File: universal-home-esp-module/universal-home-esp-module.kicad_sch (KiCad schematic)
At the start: 1 part, among them U1 ESP32-C3_SUPERMINI_SMD

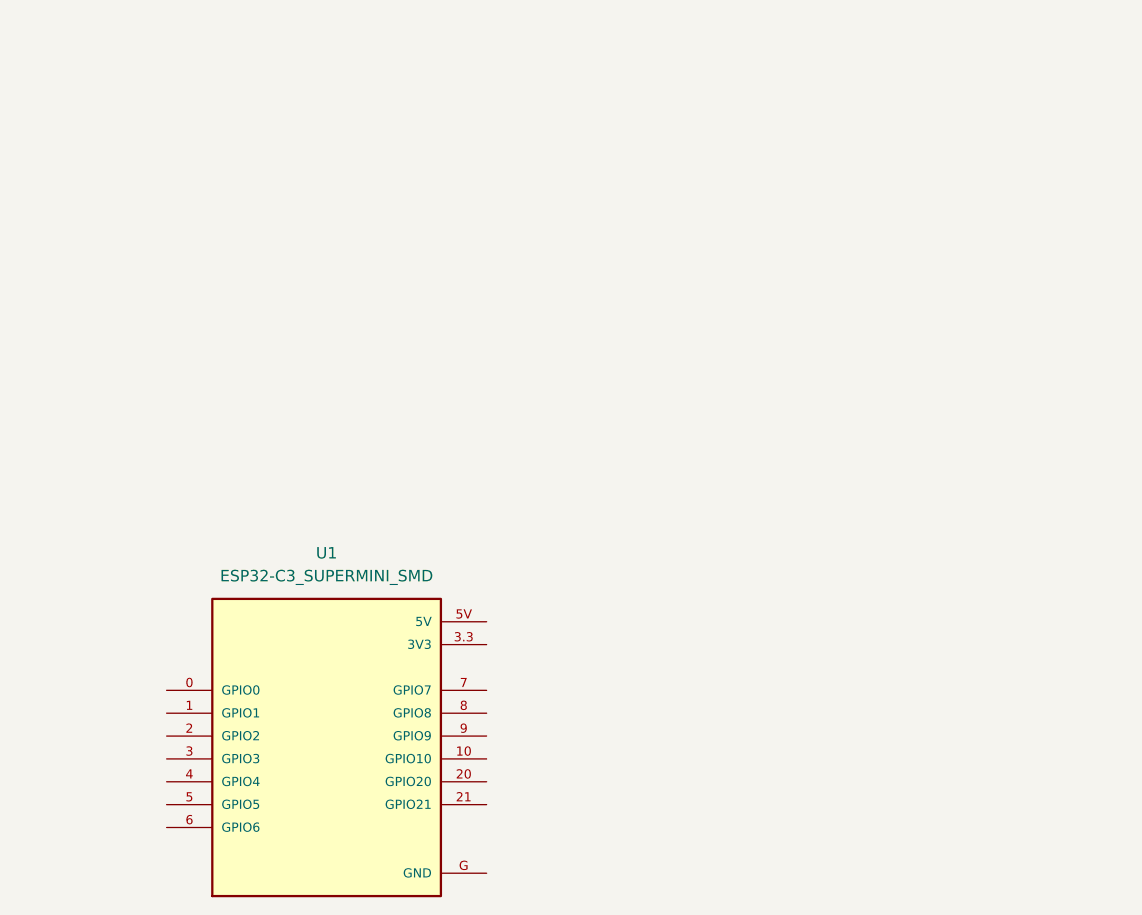
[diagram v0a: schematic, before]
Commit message: added required symbols in schematic, pending design
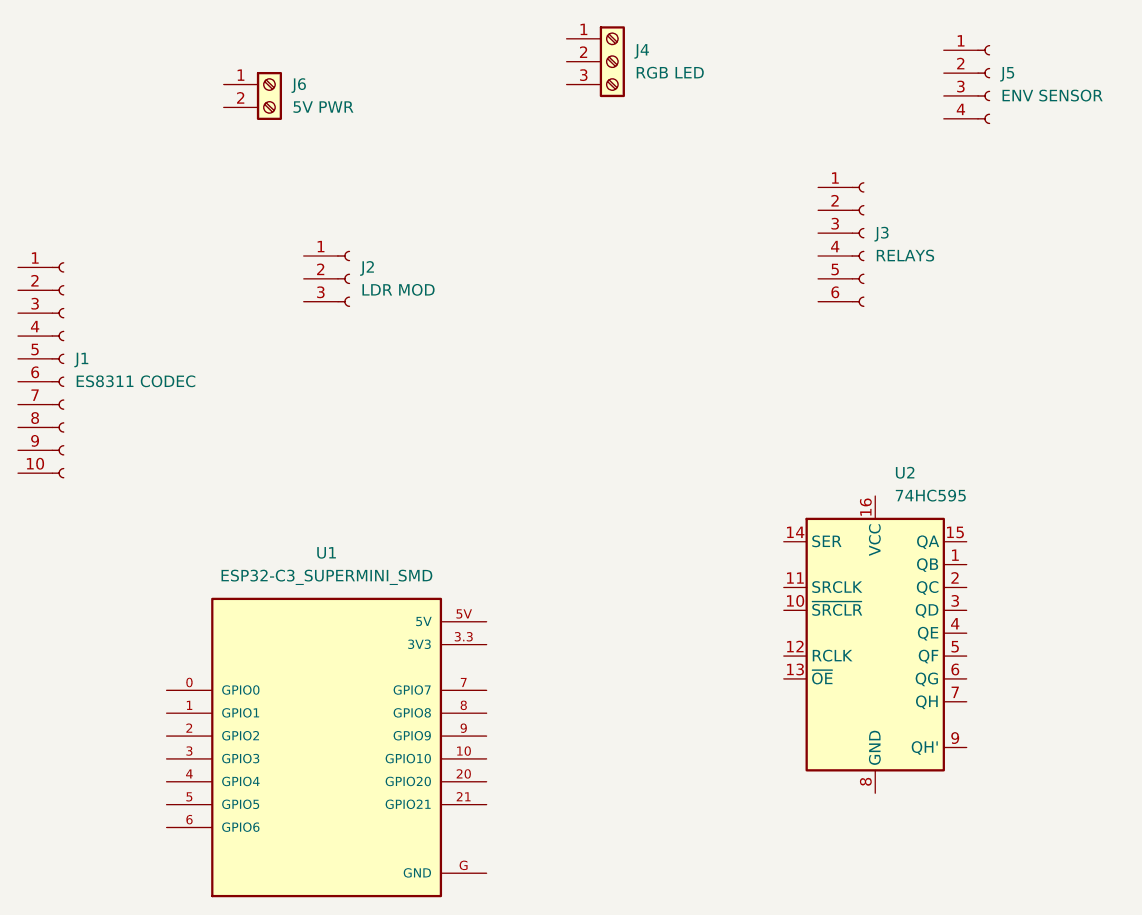
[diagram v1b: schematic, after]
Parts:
- added J1: ES8311 CODEC, Connector_PinHeader_2.54mm:PinHeader_1x10_P2.54mm_Vertical, symbol Connector:Conn_01x10_Socket
- added J2: LDR MOD, Connector_PinSocket_2.54mm:PinSocket_1x03_P2.54mm_Vertical, symbol Connector:Conn_01x03_Socket
- added J3: RELAYS, Connector_PinSocket_2.54mm:PinSocket_1x06_P2.54mm_Vertical, symbol Connector:Conn_01x06_Socket
- added J4: RGB LED, TerminalBlock_RND:TerminalBlock_RND_205-00233_1x03_P5.08mm_Horizontal, symbol Connector:Screw_Terminal_01x03
- added J5: ENV SENSOR, Connector_PinHeader_2.54mm:PinHeader_1x04_P2.54mm_Vertical, symbol Connector:Conn_01x04_Socket
- added J6: 5V PWR, TerminalBlock_RND:TerminalBlock_RND_205-00232_1x02_P5.08mm_Horizontal, symbol Connector:Screw_Terminal_01x02
- added U2: 74HC595, Package_DIP:DIP-16_W7.62mm_LongPads, symbol 74xx:74HC595

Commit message: updated schematic
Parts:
- added J7: EXT_GPIO, Connector_PinHeader_2.54mm:PinHeader_1x04_P2.54mm_Vertical, symbol Connector:Conn_01x04_Socket
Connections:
- net GND: now reaches J1.1 (Pin_1)
- net GND: now also J2.2 (Pin_2), J3.6 (Pin_6), J4.3 (Pin_3), J5.2 (Pin_2), J6.2 (Pin_2), U1.G (GND), U2.8 (GND)
- net 5V: now reaches J1.2 (Pin_2)
- net 5V: now also J6.1 (Pin_1), U1.5V
- net 3V3: now reaches J1.3 (Pin_3)
- net 3V3: now also J2.1 (Pin_1), J3.1 (Pin_1), J4.1 (Pin_1), J5.1 (Pin_1), U1.3.3 (3V3), U2.16 (VCC)
- net at U2.1 (QB): now also J3.3 (Pin_3)
- net at U2.15 (QA): now also J3.2 (Pin_2)
- net at U2.2 (QC): now also J3.4 (Pin_4)
- net at U2.3 (QD): now also J3.5 (Pin_5)
- net at U2.4 (QE): now also J7.1 (Pin_1)
- net at U2.5 (QF): now also J7.2 (Pin_2)
- net at U2.6 (QG): now also J7.3 (Pin_3)
- net at U2.7 (QH): now also J7.4 (Pin_4)
- no-connect marks 0 -> 1
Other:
- moved on the sheet: J1, J2, J3, J4, J5, J6, U2

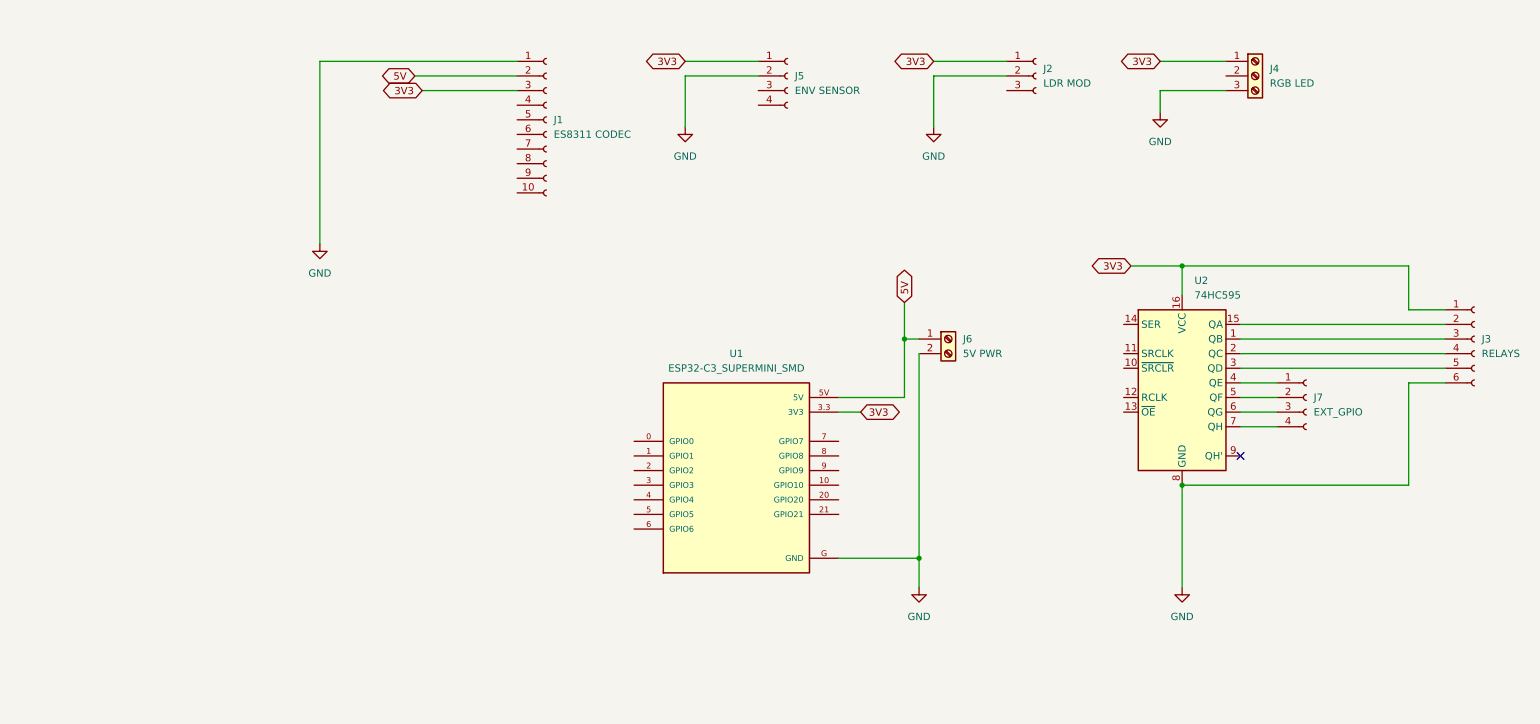
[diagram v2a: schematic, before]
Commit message: finalized schematic
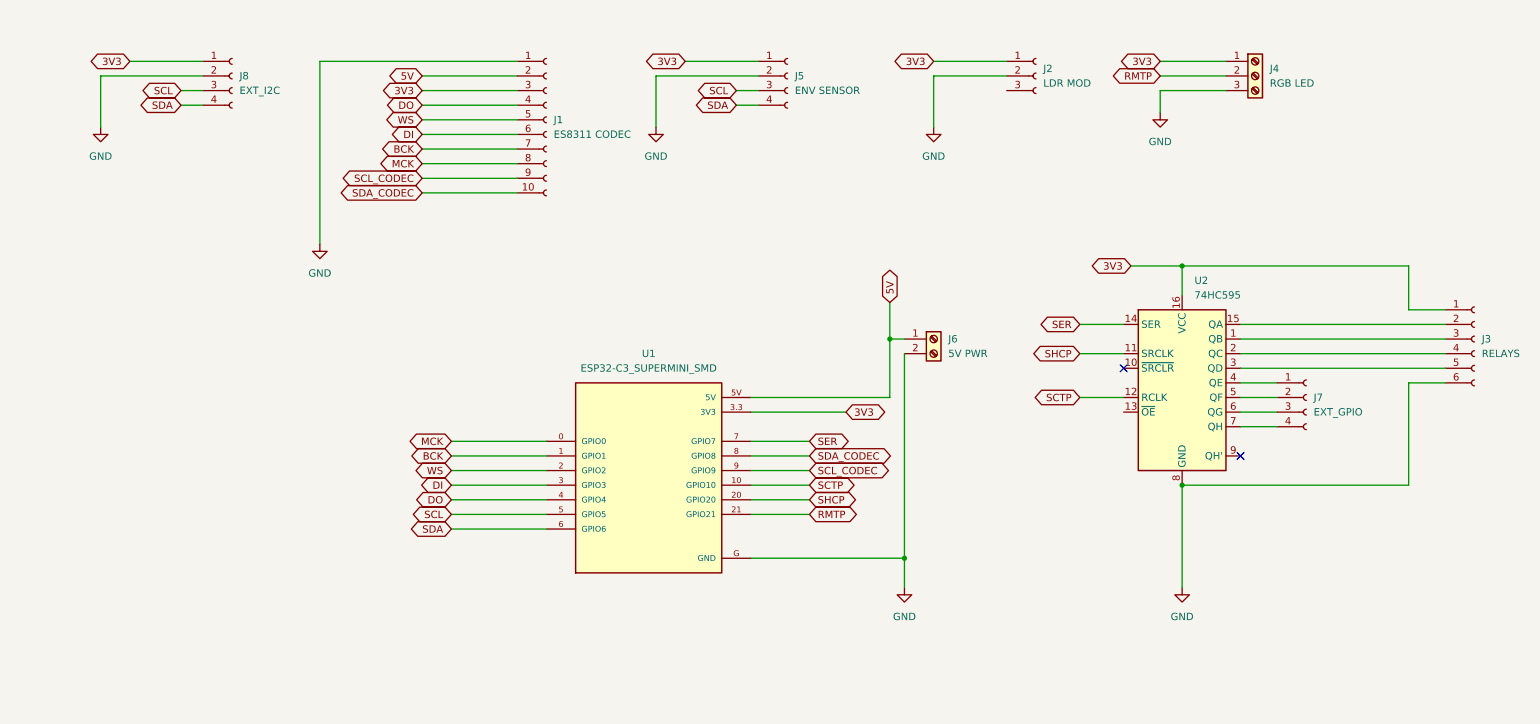
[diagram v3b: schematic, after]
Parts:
- added J8: EXT_I2C, Connector_PinHeader_2.54mm:PinHeader_1x04_P2.54mm_Vertical, symbol Connector:Conn_01x04_Socket
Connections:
- net 3V3: now also J8.1 (Pin_1)
- net GND: now also J8.2 (Pin_2)
- net SDA_CODEC: now reaches J1.10 (Pin_10)
- net SDA_CODEC: now also U1.8 (GPIO8)
- net DO: now reaches J1.4 (Pin_4)
- net DO: now also U1.4 (GPIO4)
- net WS: now reaches J1.5 (Pin_5)
- net WS: now also U1.2 (GPIO2)
- net DI: now reaches J1.6 (Pin_6)
- net DI: now also U1.3 (GPIO3)
- net BCK: now reaches J1.7 (Pin_7)
- net BCK: now also U1.1 (GPIO1)
- net MCK: now reaches J1.8 (Pin_8)
- net MCK: now also U1.0 (GPIO0)
- net SCL_CODEC: now reaches J1.9 (Pin_9)
- net SCL_CODEC: now also U1.9 (GPIO9)
- net SCTP: now reaches U1.10 (GPIO10)
- net SCTP: now also U2.12 (RCLK)
- net SHCP: now reaches U1.20 (GPIO20)
- net SHCP: now also U2.11 (SRCLK)
- net RMTP: now reaches U1.21 (GPIO21)
- net RMTP: now also J4.2 (Pin_2)
- net SCL: now reaches U1.5 (GPIO5)
- net SCL: now also J5.3 (Pin_3), J8.3 (Pin_3)
- net SDA: now reaches U1.6 (GPIO6)
- net SDA: now also J5.4 (Pin_4), J8.4 (Pin_4)
- net SER: now reaches U1.7 (GPIO7)
- net SER: now also U2.14 (SER)
- no-connect marks 1 -> 2
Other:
- moved on the sheet: J6, U1

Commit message: first pcb layout
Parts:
- added J10: ESP32_RPINS, Connector_PinSocket_2.54mm:PinSocket_1x08_P2.54mm_Vertical, symbol Connector:Conn_01x08_Pin
- added J9: ESP32_LPINS, Connector_PinSocket_2.54mm:PinSocket_1x08_P2.54mm_Vertical, symbol Connector:Conn_01x08_Pin
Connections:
- net 3V3: now also J10.3 (Pin_3); no longer J4.1 (Pin_1)
- net 5V: now also J4.1 (Pin_1), J10.1 (Pin_1)
- net BCK: now also J10.7 (Pin_7)
- net DI: now also J10.5 (Pin_5)
- net DO: now also J10.4 (Pin_4)
- net GND: now also J10.2 (Pin_2)
- net MCK: now also J10.8 (Pin_8)
- net RMTP: now also J9.8 (Pin_8)
- net SCL: now also J9.1 (Pin_1)
- net SCL_CODEC: now also J9.5 (Pin_5)
- net SCTP: now also J9.6 (Pin_6)
- net SDA: now also J9.2 (Pin_2)
- net SDA_CODEC: now also J9.4 (Pin_4)
- net SER: now also J9.3 (Pin_3)
- net SHCP: now also J9.7 (Pin_7)
- net WS: now also J10.6 (Pin_6)
